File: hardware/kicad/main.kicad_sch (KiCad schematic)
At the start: 0 parts

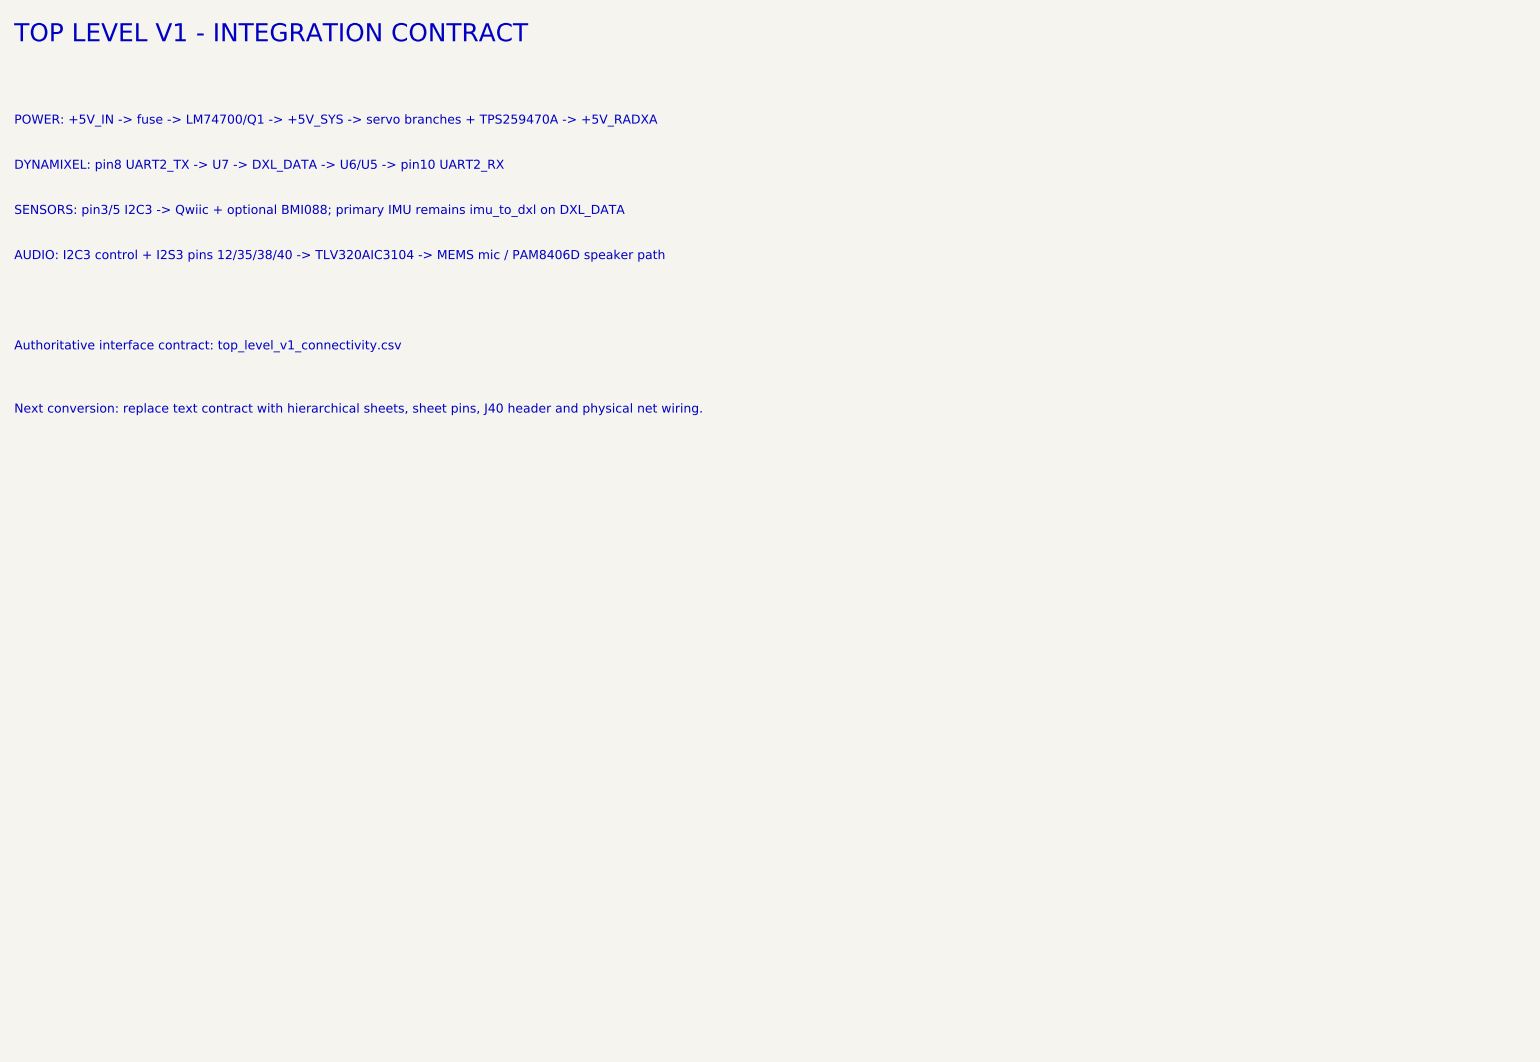
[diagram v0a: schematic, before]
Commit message: [verified] refactor(hardware): restore strict single-board Radxa port
Import the routed upstream Pollen Robot HAT as the active design, adapt the critical host nets for Radxa ZERO 3W, remove the divergent high-current redesign artifacts, and add regenerated baseline-aware KiCad validation.
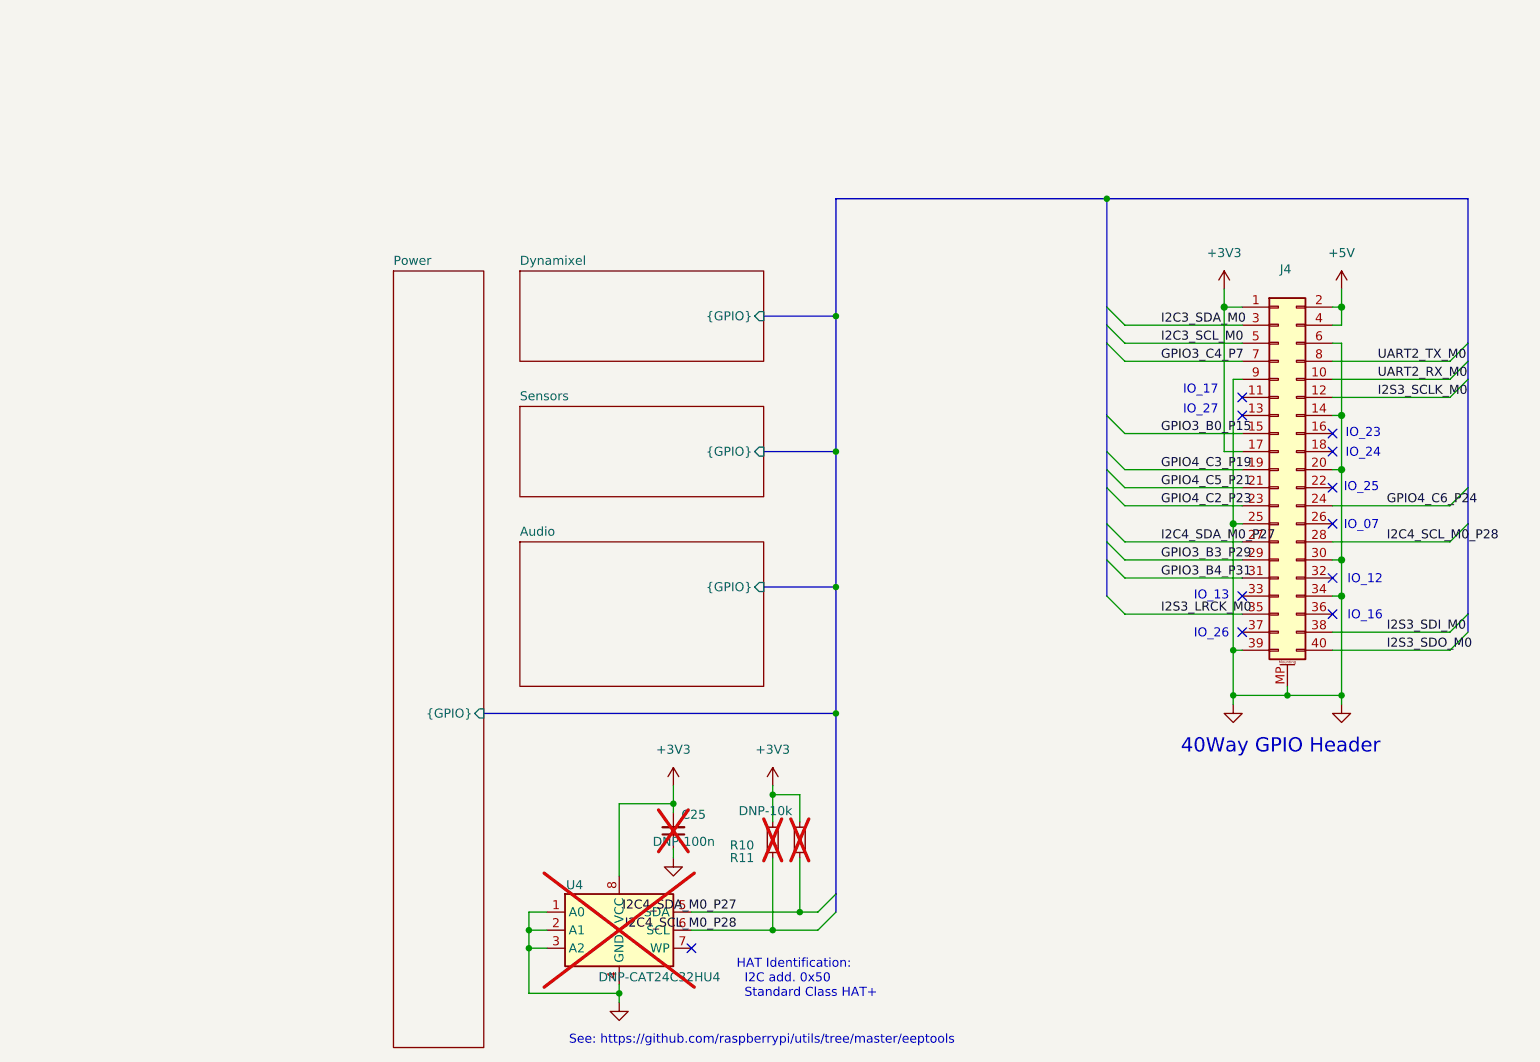
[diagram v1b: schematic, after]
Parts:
- added C25: DNP-100n, Capacitor_SMD:C_0402_1005Metric, symbol Device:C_Small
- added J4: Radxa ZERO 3W 2x20 HAT Header, Library_Pollen:PinHeader_2x20_P2.54mm_Vertical_with_rasp_HAT_zero_SMD_connector, symbol Connector_Generic_MountingPin:Conn_02x20_Odd_Even_MountingPin
- added R10, R11: DNP-10k, Resistor_SMD:R_0402_1005Metric, symbol Device:R_Small
- added U4: DNP-CAT24C32HU4, LCSC_parts_lib:TDFN-8_L3.0-W2.0-P0.50-BL-EP, symbol Memory_EEPROM:CAT24C128
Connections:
- new net +3V3: C25.2, J4.1 (Pin_1), J4.17 (Pin_17), R10.1, R11.1, U4.8 (VCC)
- new net +5V: J4.2 (Pin_2), J4.4 (Pin_4)
- new net GND: C25.1, J4.14 (Pin_14), J4.20 (Pin_20), J4.25 (Pin_25), J4.30 (Pin_30), J4.34 (Pin_34), J4.39 (Pin_39), J4.6 (Pin_6), J4.9 (Pin_9), J4.MP (MountPin), U4.1 (A0), U4.2 (A1), U4.3 (A2), U4.4 (GND)
- new net GPIO3_B0_P15: J4.15 (Pin_15)
- new net GPIO3_B3_P29: J4.29 (Pin_29)
- new net GPIO3_B4_P31: J4.31 (Pin_31)
- new net GPIO3_C4_P7: J4.7 (Pin_7)
- new net GPIO4_C2_P23: J4.23 (Pin_23)
- new net GPIO4_C3_P19: J4.19 (Pin_19)
- new net GPIO4_C5_P21: J4.21 (Pin_21)
- new net GPIO4_C6_P24: J4.24 (Pin_24)
- new net I2C3_SCL_M0: J4.5 (Pin_5)
- new net I2C3_SDA_M0: J4.3 (Pin_3)
- new net I2C4_SCL_M0_P28: J4.28 (Pin_28), R10.2, U4.6 (SCL)
- new net I2C4_SDA_M0_P27: J4.27 (Pin_27), R11.2, U4.5 (SDA)
- new net I2S3_LRCK_M0: J4.35 (Pin_35)
- new net I2S3_SCLK_M0: J4.12 (Pin_12)
- new net I2S3_SDI_M0: J4.38 (Pin_38)
- new net I2S3_SDO_M0: J4.40 (Pin_40)
- new net UART2_RX_M0: J4.10 (Pin_10)
- new net UART2_TX_M0: J4.8 (Pin_8)
- no-connect marks 0 -> 11
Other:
- added sheet Audio (audio.kicad_sch)
- added sheet Dynamixel (dynamixel.kicad_sch)
- added sheet Power (power.kicad_sch)
- added sheet Sensors (sensors.kicad_sch)
- note added: "40Way GPIO Header"
- note added: "HAT Identification: I2C add. 0x50 Standard Class HAT+"
- note added: "IO_07"
- note added: "IO_12"
- note added: "IO_13"
- note added: "IO_16"
- note added: "IO_17"
- note added: "IO_23"
- note added: "IO_24"
- note added: "IO_25"
- note added: "IO_26"
- note added: "IO_27"
- note added: "See: https://github.com/raspberrypi/utils/tree/master/eeptools"
- note removed: "AUDIO: I2C3 control + I2S3 pins 12/35/38/40 -> TLV320AIC3104 -> MEMS mic / PAM8406D speaker path"
- note removed: "Authoritative interface contract: top_level_v1_connectivity.csv"
- note removed: "DYNAMIXEL: pin8 UART2_TX -> U7 -> DXL_DATA -> U6/U5 -> pin10 UART2_RX"
- note removed: "Next conversion: replace text contract with hierarchical sheets, sheet pins, J40 header and physical net wiring."
- note removed: "POWER: +5V_IN -> fuse -> LM74700/Q1 -> +5V_SYS -> servo branches + TPS259470A -> +5V_RADXA"
- note removed: "SENSORS: pin3/5 I2C3 -> Qwiic + optional BMI088; primary IMU remains imu_to_dxl on DXL_DATA"
- note removed: "TOP LEVEL V1 - INTEGRATION CONTRACT"
- company: juper007 / DIY -> Pollen Robotics / Hugging Face
- title: Radxa ZERO 3W Robot HAT - Top Level V1 -> Radxa ZERO 3W Robot HAT

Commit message: [verified] fix(pcb): qualify J4 pass-through footprint
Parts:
- J4: Field4 Toby -> Toby Electronics; Field5 THD-20-R -> REF-182665-01; Field6 THD-20-R -> REF-182665-01; Field7 Toby -> Toby Electronics; Field8 UCON00511 -> REF-182665-01; LCSC Part C2685112 -> (none); Manufacturer_Name (none) -> Toby Electronics; Manufacturer_Part_Number (none) -> REF-182665-01; Part Description PinHeader_2x20_P2.54mm_Vertical -> 2x20 2.54 mm surface-mount bottom-entry pass-through socket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
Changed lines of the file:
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@@
 			)
 		)
-		(property "Datasheet" "~"
-			(at 198.12 80.01 0)
-			(effects
-				(font
-					(size 1.27 1.27)
-				)
-				(hide yes)
-			)
-		)
-		(property "Description" "Generic connectable mounting pin connector, double row, 02x20, odd/even pin numbering scheme (row 1 odd numbers, row 2 even numbers), script generated (kicad-library-utils/schlib/autogen/connector/)"
-			(at 198.12 80.01 0)
-			(effects
-				(font
-					(size 1.27 1.27)
-				)
-				(hide yes)
-			)
-		)
-		(property "Field4" "Toby"
-			(at 198.12 80.01 0)
-			(effects
-				(font
-					(size 1.27 1.27)
-				)
-				(hide yes)
-			)
-		)
-		(property "Field5" "THD-20-R"
-			(at 198.12 80.01 0)
-			(effects
-				(font
-					(size 1.27 1.27)
-				)
-				(hide yes)
-			)
-		)
-		(property "Field6" "THD-20-R"
-			(at 198.12 80.01 0)
-			(effects
-				(font
-					(size 1.27 1.27)
-				)
-				(hide yes)
-			)
-		)
-		(property "Field7" "Toby"
-			(at 198.12 80.01 0)
-			(effects
-				(font
-					(size 1.27 1.27)
-				)
-				(hide yes)
-			)
-		)
-		(property "Field8" "UCON00511"
-			(at 198.12 80.01 0)
-			(effects
-				(font
-					(size 1.27 1.27)
-				)
-				(hide yes)
-			)
-		)
-		(property "Part Description" "PinHeader_2x20_P2.54mm_Vertical"
+		(property "Datasheet" "https://www.toby.co.uk/board-to-board-pcb-connectors/254mm-sockets/ref-raspberry-pi-rpi-hat-specification-connector-surface-mount-sockets/REF-182665-01"
+			(at 198.12 80.01 0)
+			(effects
+				(font
+					(size 1.27 1.27)
+				)
+				(hide yes)
+			)
+		)
+		(property "Description" "2x20 2.54 mm surface-mount bottom-entry pass-through socket with PCB pegs"
+			(at 198.12 80.01 0)
+			(effects
+				(font
+					(size 1.27 1.27)
+				)
+				(hide yes)
+			)
+		)
+		(property "Field4" "Toby Electronics"
+			(at 198.12 80.01 0)
+			(effects
+				(font
+					(size 1.27 1.27)
+				)
+				(hide yes)
+			)
+		)
+		(property "Field5" "REF-182665-01"
+			(at 198.12 80.01 0)
+			(effects
+				(font
+					(size 1.27 1.27)
+				)
+				(hide yes)
+			)
+		)
+		(property "Field6" "REF-182665-01"
+			(at 198.12 80.01 0)
+			(effects
+				(font
+					(size 1.27 1.27)
+				)
+				(hide yes)
+			)
+		)
+		(property "Field7" "Toby Electronics"
+			(at 198.12 80.01 0)
+			(effects
+				(font
+					(size 1.27 1.27)
+				)
+				(hide yes)
+			)
+		)
+		(property "Field8" "REF-182665-01"
+			(at 198.12 80.01 0)
+			(effects
+				(font
+					(size 1.27 1.27)
+				)
+				(hide yes)
+			)
+		)
+		(property "Part Description" "2x20 2.54 mm surface-mount bottom-entry pass-through socket with PCB pegs"
 			(at 198.12 80.01 0)
 			(effects
@@
 			)
 		)
-		(property "Manufacturer_Name" ""
-			(at 198.12 80.01 0)
-			(effects
-				(font
-					(size 1.27 1.27)
-				)
-				(hide yes)
-			)
-		)
-		(property "Manufacturer_Part_Number" ""
+		(property "Manufacturer_Name" "Toby Electronics"
+			(at 198.12 80.01 0)
+			(effects
+				(font
+					(size 1.27 1.27)
+				)
+				(hide yes)
+			)
+		)
+		(property "Manufacturer_Part_Number" "REF-182665-01"
 			(at 198.12 80.01 0)
 			(effects
@@
 			)
 		)
-		(property "LCSC Part" "C2685112"
-			(at 198.12 80.01 0)
-			(effects
+		(property "LCSC Part" ""
+			(at 198.12 80.01 0)
+			(effects

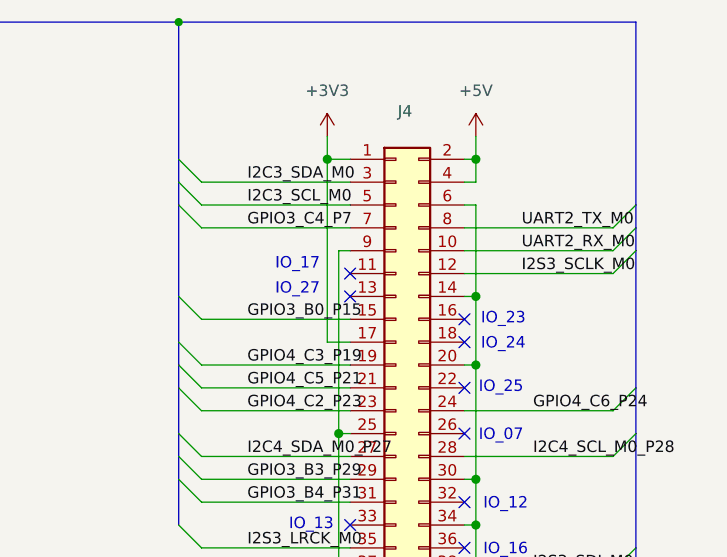
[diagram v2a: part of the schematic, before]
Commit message: [verified] fix(hardware): correct power bias and default-off GPIO controls
Qualify Q2 land and gate rating, battery-bias LM5050 VS, and correct C39 identity. Add host-referenced active-low battery sensing and default-off amplifier control while preserving connector parity. Expand exact regression guards and complete BOM/position exports. Fabrication approval remains pending physical and runtime validation.
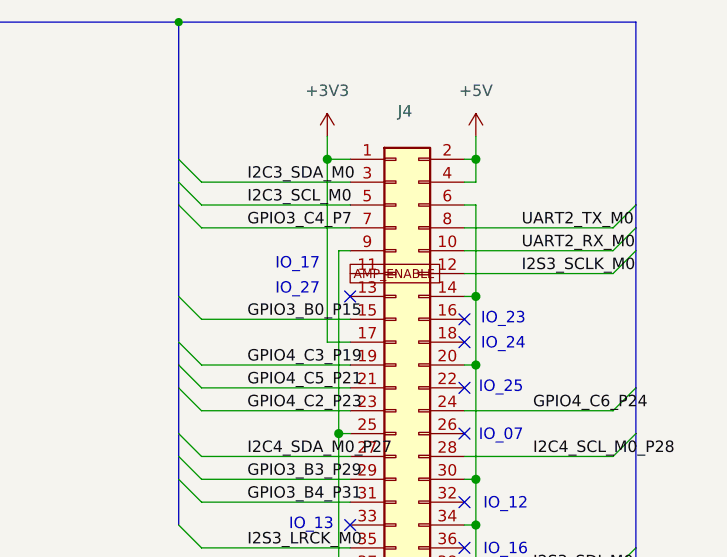
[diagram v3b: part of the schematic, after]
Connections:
- net AMP_ENABLE: now reaches J4.11 (Pin_11)
- no-connect marks 11 -> 10
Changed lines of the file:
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@@
 	)
 	(no_connect
-		(at 193.04 69.85)
-	)
-	(no_connect
 		(at 205.74 77.47)
 	)
@@
 		)
 	)
+	(global_label "AMP_ENABLE" (shape passive) (at 193.04 69.85 0) (effects (font (size 1.0 1.0)) (justify left)) (property "Intersheetrefs" "${INTERSHEET_REFS}" (at 193.04 69.85 0) (effects (font (size 1 1)) (hide yes))))
 )
